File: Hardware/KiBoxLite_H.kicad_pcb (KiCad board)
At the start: 4 copper layers, 49.6 x 86.5 mm, 163 parts, among them J1 Screw_Terminal_01x03, J2 USB4105-GF-A-060, Q2 BC817-40(SOT23), Q3 BC817-40(SOT23), T1 LMUN2211LT1G(SOT-23), U1 CH340X(MSOP-10), U10 MAX13487, U3 TP4054-42-SOT25-R(SOT23-5), U4 LAN8710A-EZC(QFN32), U5 TX4138(ESOIC-8), U6 ESP32-WROOM-32E-N4, U7 TPS62A02ADRLR(SOT-563-6), U8 NA(SN74LVC1G04DBVR(SOT23-5)), U9 TPS2378DDAR(HSOIC-8)

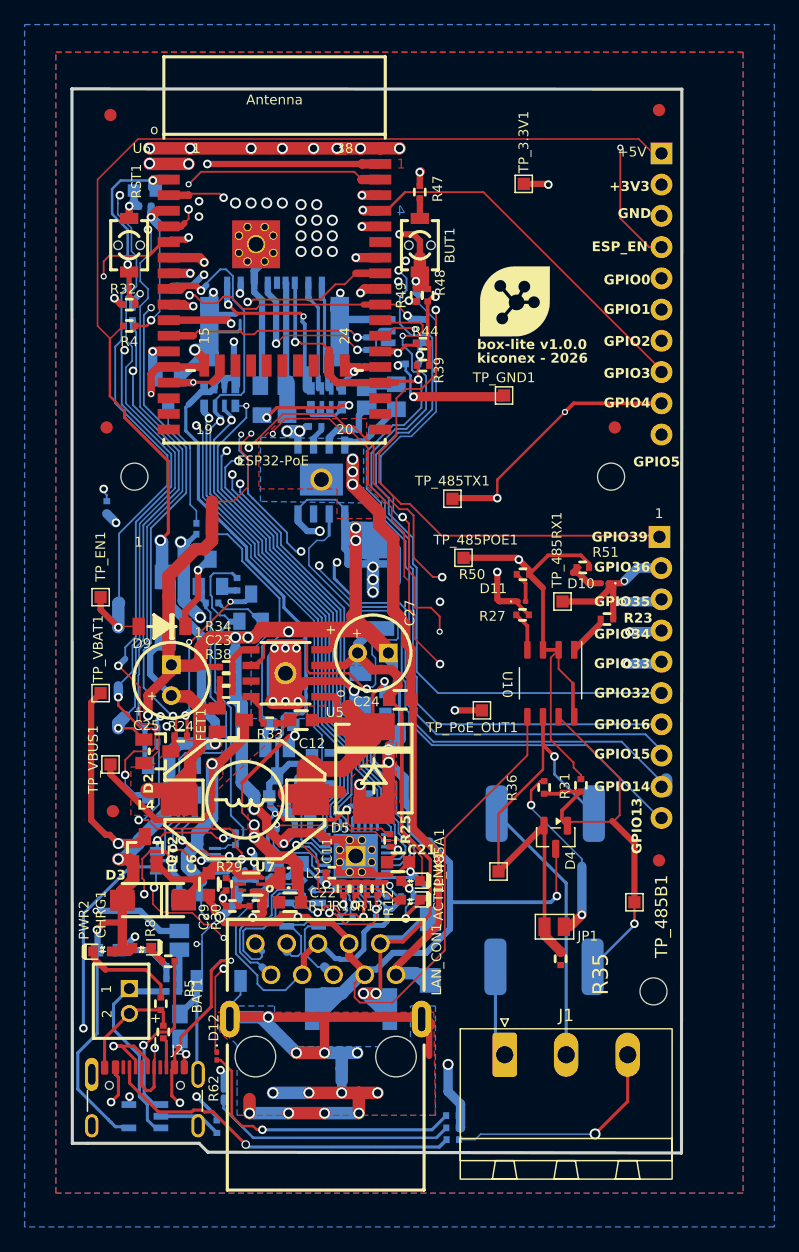
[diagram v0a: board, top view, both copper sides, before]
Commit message: build: rj45 con leds
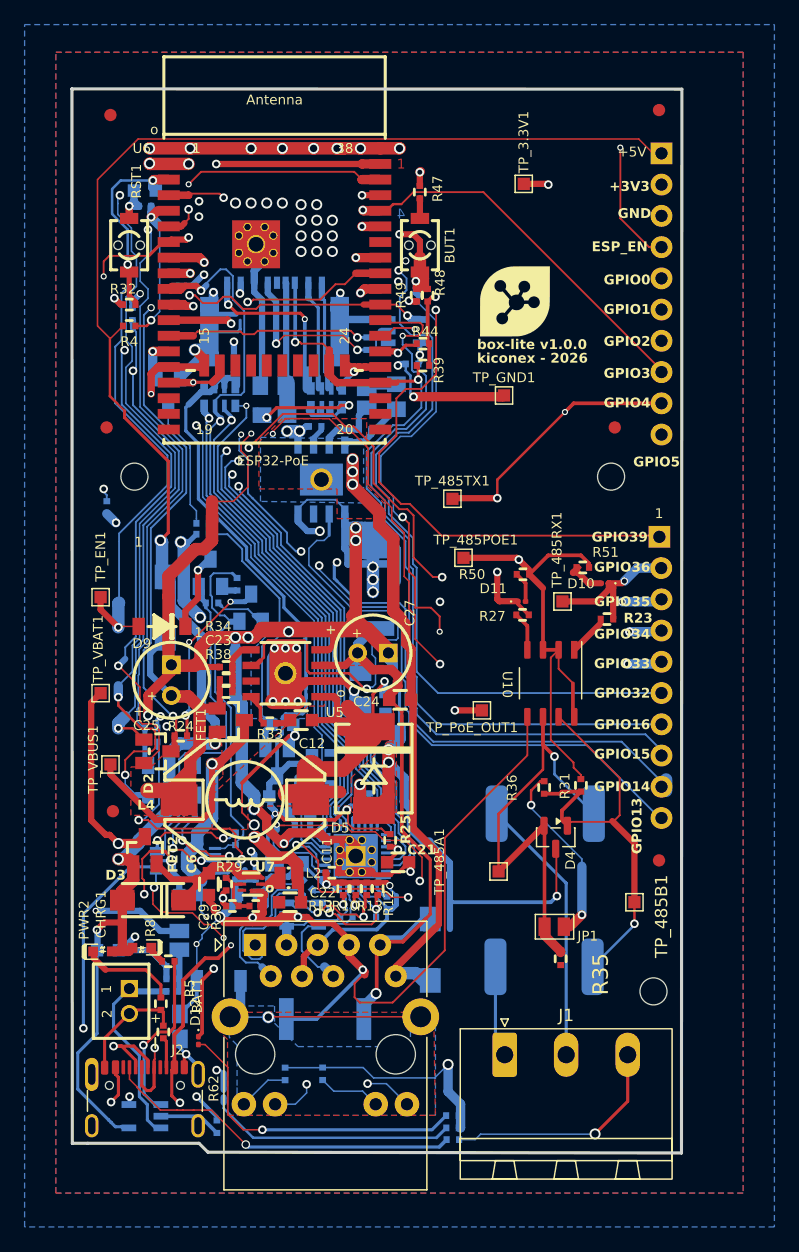
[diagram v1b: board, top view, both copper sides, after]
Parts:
- removed ACT1: LED/YELLOW/0603, OLIMEX_LEDs-FP:LED_0603_KA
- removed LAN_CON1: RJP-003TC1(LPJ4112CNL), OLIMEX_Connectors-FP:RJP-003TC1(LPJ4112CNL)
- removed LNK1: LED/GREEN/0603, OLIMEX_LEDs-FP:LED_0603_KA
- removed R14, R15: 2.2k/R0402, OLIMEX_RLC-FP:R_0402_5MIL_DWS
- added J3: RJ45_Abracon_ARJP11A-MASA-B-A-EMU2, Connector_RJ:RJ45_Abracon_ARJP11A-MA_Horizontal, F.Cu at (102.6, 156.1)
- added R57: 2.2k/R0402, OLIMEX_RLC-FP:R_0402_5MIL_DWS, B.Cu at (108.0, 166.6)
- added R58: 2.2k/R0402, OLIMEX_RLC-FP:R_0402_5MIL_DWS, B.Cu at (105.0, 166.6)
- moved R7 2.26 mm to (108.2, 162.1)
- moved D12 1.95 mm to (98.0, 163.8)
- turned C2 to 180 degrees
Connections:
- C2 pad 1: GND -> Net-(C2-Pad1)
- C2 pad 2: Net-(LAN_CON1-Shield) -> GND
- U4 pad 2: Net-(LNK1-K) -> /Led2
- U4 pad 3: Net-(ACT1-A) -> /Led1
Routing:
- net Net-(LAN_CON1-Shield): track 64.0 -> 0.00 mm, vias 12 -> 0
- net /Led2: track 0.00 -> 44.6 mm, vias 0 -> 3
- net /Led1: track 0.00 -> 38.1 mm, vias 0 -> 3
- net Net-(LNK1-K): track 22.5 -> 0.00 mm, vias 1 -> 0
- net GND: track 546.8 -> 526.3 mm, vias 62 -> 63
- net Net-(C2-Pad1): track 0.00 -> 19.5 mm, vias 0 -> 1
- net Net-(ACT1-A): track 15.3 -> 0.00 mm, vias 1 -> 0
- net Net-(J3-RCT): track 47.8 -> 32.5 mm
- net +3.3V: track 262.6 -> 277.4 mm
- net Spare1: track 82.1 -> 75.7 mm, vias 4 -> 3
- net Net-(J3-Pad13): track 0.00 -> 5.13 mm
- net Net-(ACT1-K): track 4.85 -> 0.00 mm, vias 1 -> 0
- net Net-(J3-Pad11): track 0.00 -> 4.17 mm
- net /RD+: track 13.2 -> 10.1 mm
- net Net-(D12-A): track 23.6 -> 25.7 mm
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- removed copper zone on B.Cu, net Net-(LAN_CON1-Shield)
- removed copper zone on F.Cu, net Net-(LAN_CON1-Shield)
- removed copper zone on In1.Cu, net Net-(LAN_CON1-Shield)
- removed copper zone on In2.Cu, net Net-(LAN_CON1-Shield)

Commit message: build: optimizacion pcb
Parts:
- FID2, FID5, FID6: moved to B.Cu
- moved FID5 24.3 mm to (135.6, 90.0), turned to 180 degrees
- moved FID2 24.0 mm to (90.4, 90.0), turned to 180 degrees
- moved 3.3V1 10.2 mm to (119.4, 103.1)
- moved 485TX1 5.80 mm to (124.4, 120.0)
- moved 485RX1 5.25 mm to (128.8, 123.0)
- moved 485POE1 5.14 mm to (124.4, 123.0)
- moved MH2 3.75 mm to (127.8, 118.1)
- moved FID6 3.63 mm to (134.7, 152.8), turned to 180 degrees
- moved 485A1 2.67 mm to (121.0, 152.4)
- moved EN1 2.45 mm to (90.0, 125.3)
- moved EXT1 2.28 mm to (135.6, 105.4)
- moved D10 2.09 mm to (129.1, 127.7)
- moved 485B1 1.96 mm to (131.4, 152.4)
- moved FID3 1.79 mm to (135.6, 90.0)
- moved R1 1.67 mm to (89.8, 122.0)
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- renumbered TP_3.3V1 to 3.3V1, TP_485A1 to 485A1, TP_485B1 to 485B1, TP_485POE1 to 485POE1, TP_485RX1 to 485RX1, TP_485TX1 to 485TX1, TP_EN1 to EN1, TP_GND1 to GND1, TP_PoE_OUT1 to PoE1, TP_VBAT1 to VBAT1, TP_VBUS1 to VBUS1
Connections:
- EXT1 pad 1: +5V -> /GPIO16\I2C-SCL
- EXT2 pad 7: /GPIO16\I2C-SCL -> +5V
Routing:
- net +5V: track 227.7 -> 96.0 mm, vias 6 -> 8
- net GND: track 526.3 -> 448.3 mm, vias 63 -> 66
- net +3.3V: track 277.4 -> 205.0 mm, vias 15 -> 14
- net /GPIO16\I2C-SCL: track 85.4 -> 55.5 mm
- net /485_TX: track 53.6 -> 68.6 mm, vias 4 -> 2
- net /GPIO5\SPI_CS: track 67.6 -> 54.2 mm
- net /485_RX: track 84.1 -> 95.6 mm, vias 4 -> 3
- net /GPI39: track 78.7 -> 73.7 mm
- net /GPIO3\U0RXD: track 103.2 -> 108.0 mm
- net /GPIO32: track 79.8 -> 84.2 mm
- net /TD+: track 25.0 -> 21.8 mm
- net /ESP_EN: track 106.1 -> 109.1 mm, vias 4 -> 3
- net /GPIO0: track 97.0 -> 95.0 mm
- net Net-(D10-A): track 3.51 -> 1.74 mm
- net /GPI34\BUT1: track 85.9 -> 84.1 mm, vias 6 -> 5
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- added copper zone on In2.Cu, net +5V
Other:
- board size 49.6 x 86.5 mm -> 50 x 85 mm

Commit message: build: gerbers pcb
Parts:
- moved R57 2.97 mm to (110.2, 168.7)
- moved J1 2.10 mm to (122.8, 162.9)
- moved MH3 1.60 mm to (134.9, 158.2)
- moved J3 1.45 mm to (102.6, 157.5)
- moved F1 1.37 mm to (126.1, 156.5)
- moved R7 1.05 mm to (108.2, 163.2)
- moved C2 0.65 mm to (99.6, 159.7)
- moved J2 0.50 mm to (93.5, 170.2)
- moved R58 0.50 mm to (105.5, 166.6)
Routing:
- net GND: track 448.3 -> 467.8 mm, vias 66 -> 65
- net +3.3V: track 205.0 -> 213.6 mm
- net /TD-: track 25.9 -> 20.2 mm
- net /TD+: track 21.8 -> 17.9 mm
- net Net-(J3-Pad13): track 5.13 -> 2.76 mm
- net Net-(J1-Pin_2): track 22.1 -> 20.0 mm
- net Net-(J1-Pin_1): track 7.46 -> 5.36 mm
- net Spare1: track 75.7 -> 77.5 mm, vias 3 -> 2
- net /485_B: track 36.4 -> 34.6 mm
- net VBUS: track 65.6 -> 67.2 mm
- net /RD+: track 10.1 -> 11.6 mm
- net Net-(D13-A): track 20.3 -> 21.6 mm
- net Net-(C2-Pad1): track 19.5 -> 20.7 mm, vias 1 -> 0
- net Net-(J3-Pad11): track 4.17 -> 5.25 mm
- net Net-(D12-A): track 25.7 -> 24.9 mm
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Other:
- outline, holes or cut-outs redrawn
